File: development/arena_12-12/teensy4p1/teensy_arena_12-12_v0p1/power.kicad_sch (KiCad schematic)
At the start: 2 parts, among them J1 Barrel_Jack, SW1 SW_SPDT

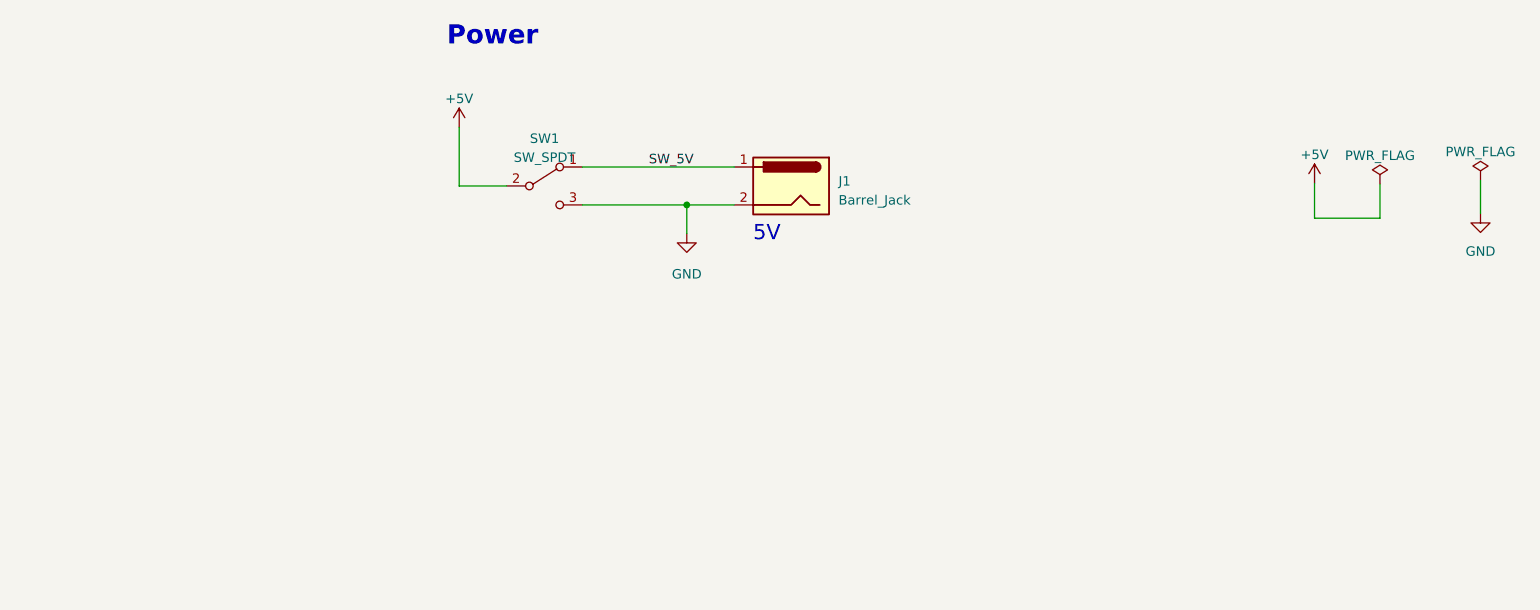
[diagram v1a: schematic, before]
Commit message: More work on schematic for 12-12 teensy arena.
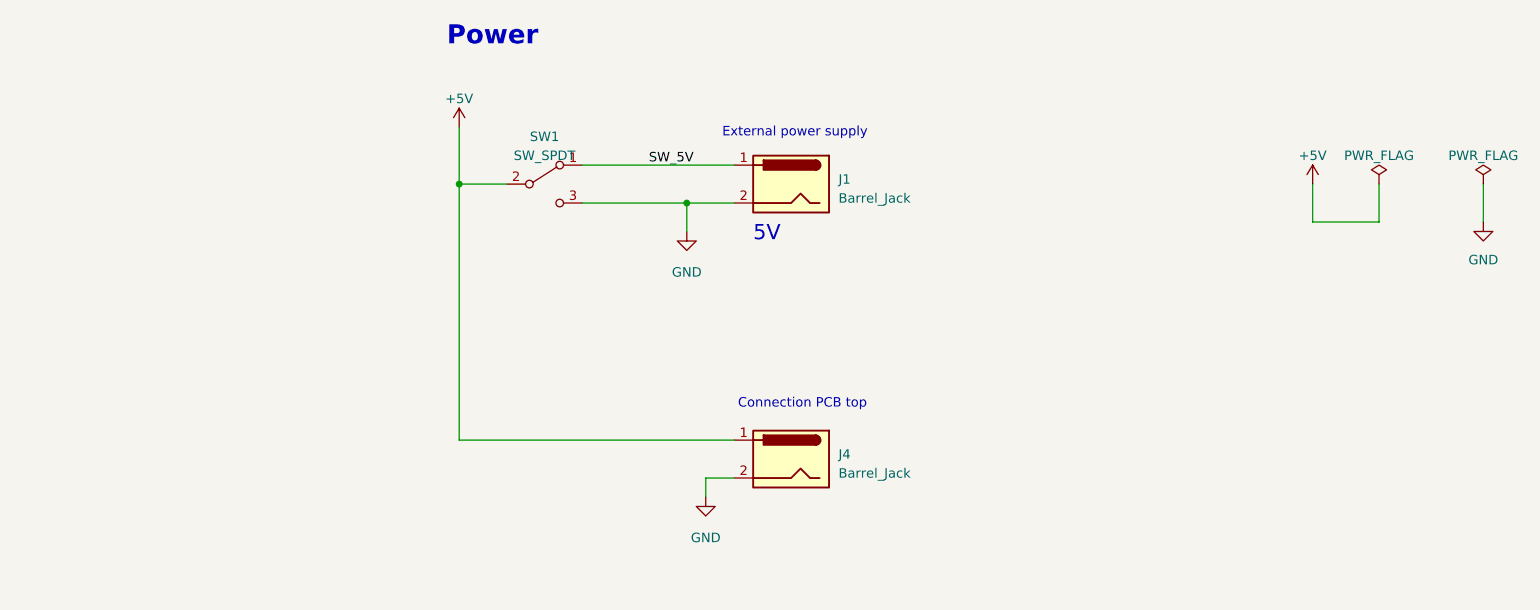
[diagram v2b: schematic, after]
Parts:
- added J4: Barrel_Jack, arena_custom:DCJACK_2PIN_HIGHCURRENT, symbol Connector:Barrel_Jack
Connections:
- net +5V: now also J4.1
- net GND: now also J4.2
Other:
- note added: "Connection PCB top"
- note added: "External power supply"

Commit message: Added source termination resistors to miso lines.
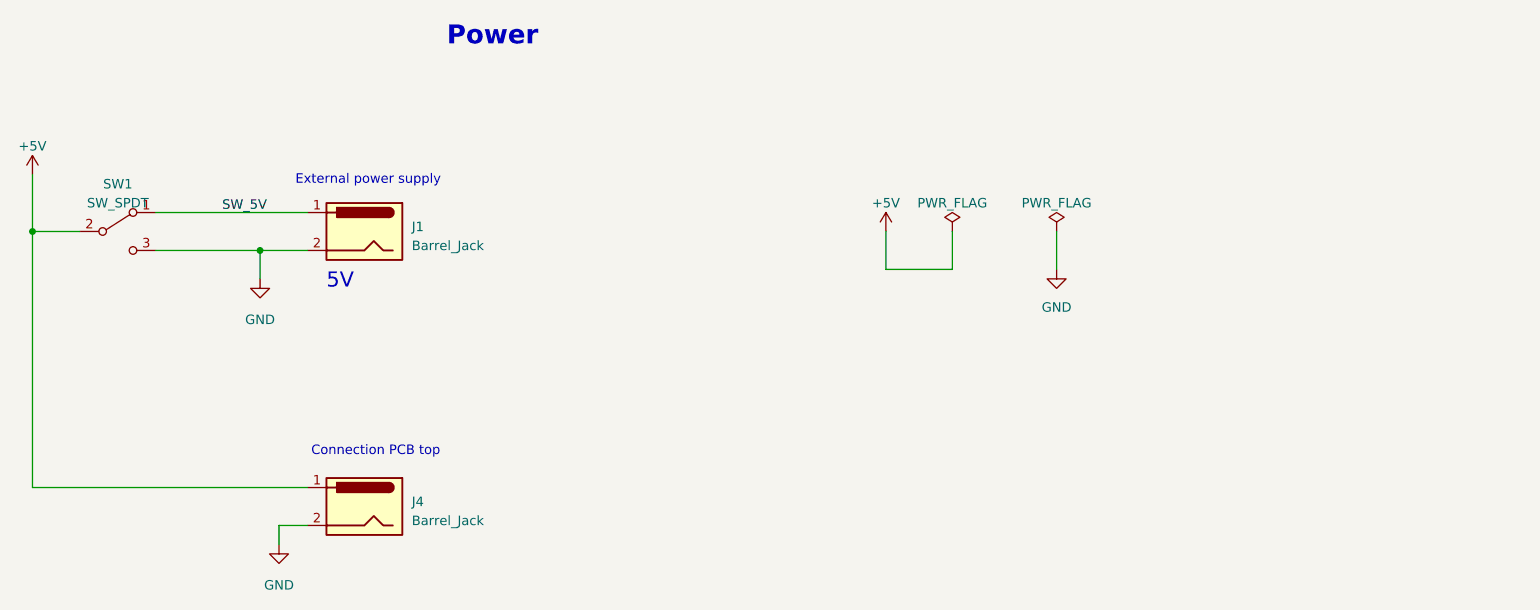
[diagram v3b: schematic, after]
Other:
- moved on the sheet: J1, J4, SW1
